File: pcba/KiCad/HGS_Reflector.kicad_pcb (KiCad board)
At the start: 4 copper layers, 100 x 100 mm, 64 parts, among them J1 U.FL, J2 USB_MINI-B_SMT, J3 SM06B-SRSS-TB(LF)(SN), J5 132134-10, J6 132134-10, T1 QWT2.4222, U1 LP2985XX-N, U2 LP2985XX-N, U3 NCS3-272+, U4 QPQ1907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

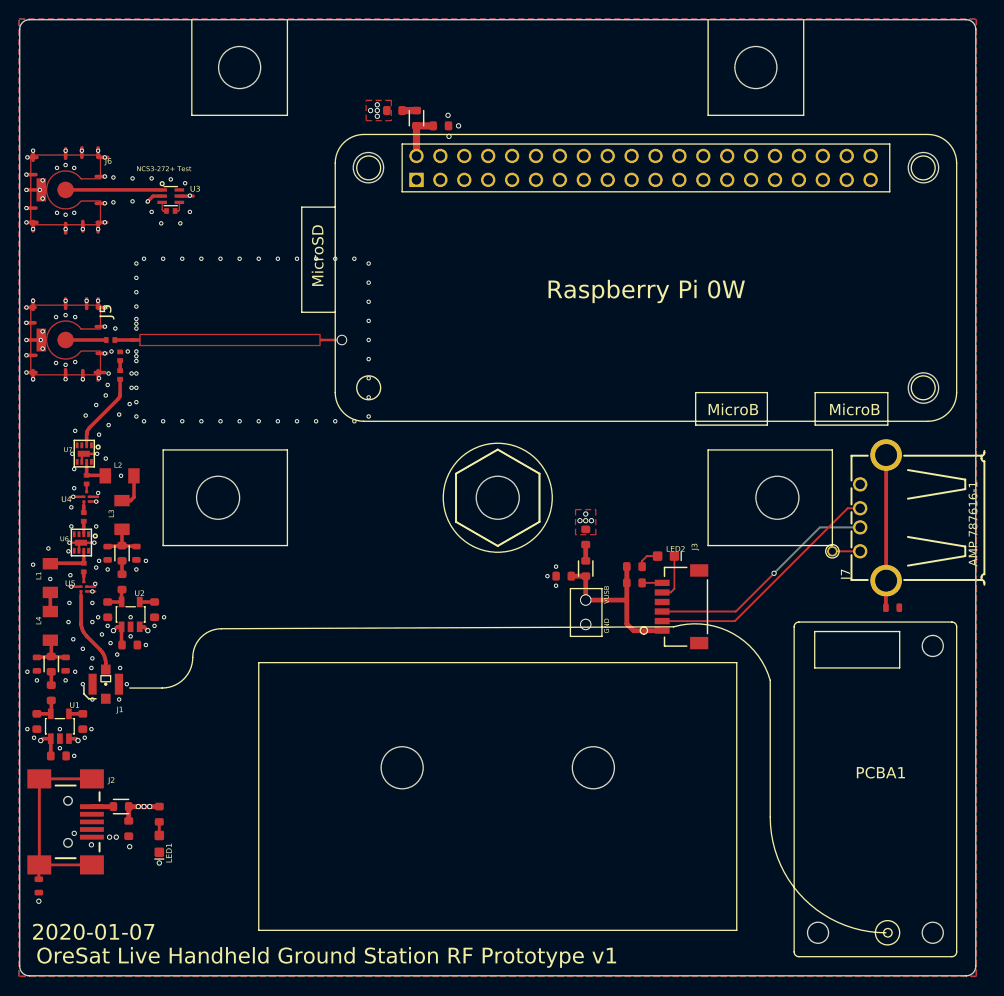
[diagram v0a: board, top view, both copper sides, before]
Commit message: fixed reference designators, fixed symbol/footprint pads and pins, added impedance matching at helical
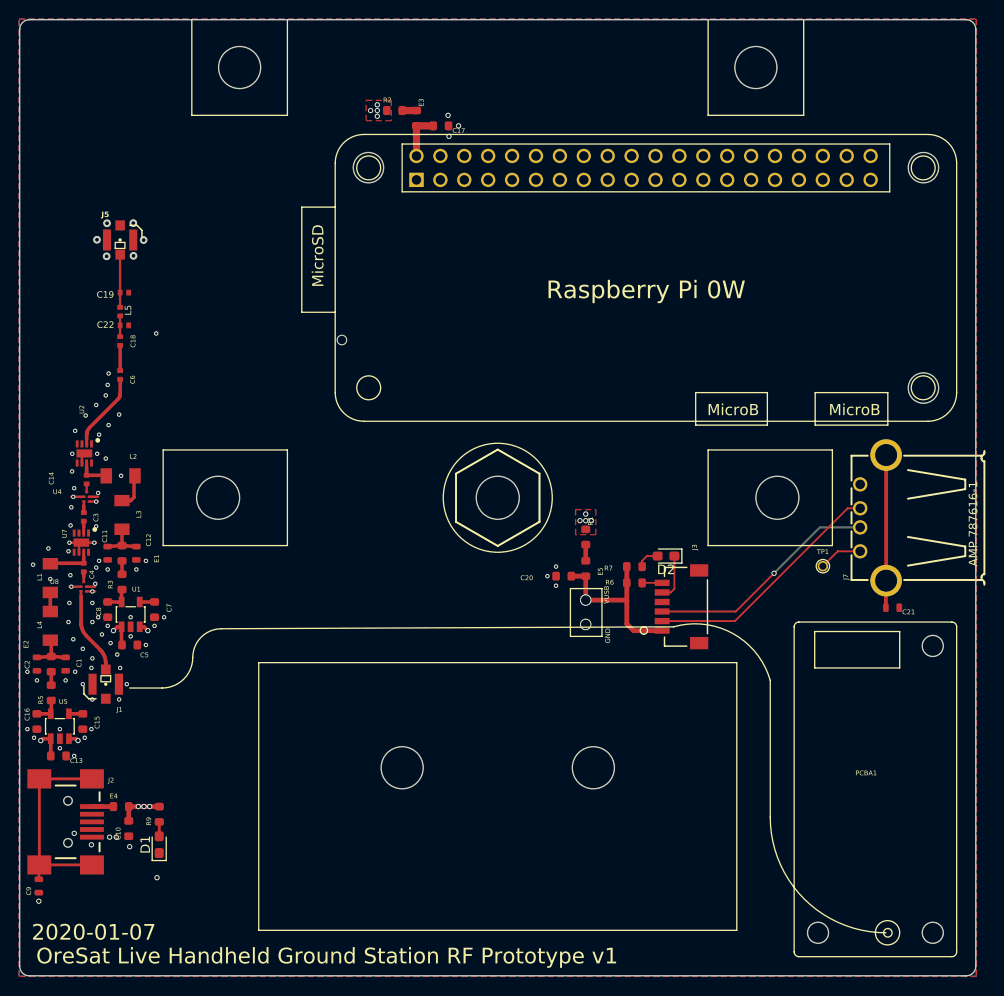
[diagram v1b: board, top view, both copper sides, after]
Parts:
- removed J6: 132134-10, HGS_Reflector:132134-10
- removed LED1, LED2: GREEN, HGS_Reflector:LED-0603
- removed R4: 150, HGS_Reflector:.0402-C-NOSILK
- removed T1: QWT2.4222, HGS_Reflector:QWT_2.422G-V2
- removed TP2: TEST-POINT-LARGE-SQUARE, HGS_Reflector:1X01
- removed U3: NCS3-272+, HGS_Reflector:GE0805C-1
- added C22: 1.0 pF, oresat-passives:0402-C-NOSILK, F.Cu at (109.5, 87.0)
- added D1: Green, LED_SMD:LED_0603_1608Metric_Pad1.05x0.95mm_HandSolder, F.Cu at (113.1, 141.3)
- added D2: Green, LED_SMD:LED_0603_1608Metric_Pad1.05x0.95mm_HandSolder, F.Cu at (166.1, 111.1)
- added L5: 4.3 nH, oresat-passives:0402-C-NOSILK, F.Cu at (109.0, 85.5)
- added TP1: Test-Point, oresat-misc:TestPoint-0.75mm-th, F.Cu at (182.5, 112.2)
- C1, C11, C12, C2, C21, C9: footprint HGS_Reflector:.0603-C-NOSILK -> oresat-passives:0603-C-NOSILK
- C10, C13, C15, C16, C17, C20, C5, C7, C8, R1, R2, R3, R5, R6, R7, R9: footprint HGS_Reflector:.0603-B-NOSILK -> oresat-passives:0603-B-NOSILK
- C14, C18, C3, C4, C6: footprint HGS_Reflector:.0402-C-NOSILK -> oresat-passives:0402-C-NOSILK
- C19: value 100 pF -> 0.9 pF; footprint HGS_Reflector:.0402-C-NOSILK -> oresat-passives:0402-C-NOSILK
- E1, E2, E3, E4, E5: footprint HGS_Reflector:.0603-B -> oresat-passives:0603-B-NOSILK
- J1: footprint HGS_Reflector:U.FL -> oresat-connectors:U.FL
- J2: value USB_MINI-B_SMT -> USB_C_Plug_USB2.0; footprint HGS_Reflector:USB-MINIB -> oresat-connectors:USB-MINIB
- J3: footprint HGS_Reflector:CONN_SM06B-SRSS-TB_JST -> oresat-connectors:CONN_SM06B-SRSS-TB_JST
- J5: footprint HGS_Reflector:132134-10 -> oresat-connectors:U.FL
- J7: value (none) -> USB_HOST_W/CHASSIS_GND; footprint HGS_Reflector:GHI2_USB_HOST_HORIZONTAL_W_CHASSIS_GND -> oresat-misc:GHI2_USB_HOST_HORIZONTAL_W_CHASSIS_GND
- L1, L2, L3, L4: footprint HGS_Reflector:L3216C -> oresat-passives:L3216C
- PCBA2: value (none) -> RASP_PI_0WPI_0W; footprint HGS_Reflector:RASP_PI_0W -> oresat-misc:RASP_PI_0W
- U1: renamed from U2; value LP2985XX-N -> LP2985-N; footprint HGS_Reflector:SOT-23 -> oresat-ics:SOT-23 LP2985
- U2: renamed from U7; value LNA-TP3M9037 -> TQP3M9037; footprint HGS_Reflector:TP3M9037 -> oresat-ics:TQP3M9037
- U4: footprint HGS_Reflector:QPQ1907 -> oresat-ics:QPQ1907
- U5: renamed from U1; value LP2985XX-N -> LP2985-N; footprint HGS_Reflector:SOT-23 -> oresat-ics:SOT-23 LP2985
- U7: renamed from U6; value LNA-TP3M9037 -> TQP3M9037; footprint HGS_Reflector:TP3M9037 -> oresat-ics:TQP3M9037
- U8: renamed from U5; value QPQ1907 -> B39162B9417K610; footprint HGS_Reflector:QPQ1907 -> oresat-ics:QPQ1907
- moved J5 11.9 mm to (109.0, 78.0)
- moved C19 6.68 mm to (109.5, 83.5), turned to 180 degrees
- moved C18 1.00 mm to (109.0, 88.6), turned to 90 degrees
- moved L2 0.11 mm to (109.1, 102.7)
- moved U2 0.07 mm to (105.3, 100.4), turned to -90 degrees
- turned U7 to -90 degrees
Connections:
- net N$12 renamed VBUS
- C14 pad 1: N$16 -> Net-(U2-RF_OUT)
- C14 pad 2: N$26 -> Net-(U4-IN)
- C18 pad 1: HELICAL -> Net-(C18-Pad1)
- C18 pad 2: T1-50 -> Net-(C18-Pad2)
- C19 pad 2: N$9 -> Net-(J5-SIGNAL)
- C3 pad 1: N$4 -> Net-(U4-OUT)
- C3 pad 2: N$8 -> Net-(U7-RF_IN)
- C4 pad 1: N$13 -> Net-(U7-RF_OUT)
- C4 pad 2: N$3 -> Net-(U8-IN)
- C6 pad 1: N$9 -> Net-(C18-Pad1)
- C6 pad 2: N$11 -> Net-(U2-RF_IN)
- C9 pad 2: KEEPOUT -> Net-(J2-SHIELD)
- E4 pad 1: VUSB -> Net-(E4-Pad1)
- J1 pad FEED: N$5 -> Net-(J1-SIGNAL)
- J2 pad S1: KEEPOUT -> Net-(J2-SHIELD)
- L1 pad 1: N$13 -> Net-(U7-RF_OUT)
- L2 pad 1: N$16 -> Net-(U2-RF_OUT)
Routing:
- net GND: track 49.6 -> 10.9 mm, vias 201 -> 91
- net Net-(J2-SHIELD): track 0.00 -> 24.0 mm
- net KEEPOUT: track 24.0 -> 0.00 mm
- net N$23: track 10.1 -> 0.00 mm
- net Net-(J1-SIGNAL): track 0.00 -> 9.10 mm
- net N$5: track 9.10 -> 0.00 mm
- net Net-(U2-RF_IN): track 0.00 -> 8.29 mm
- net N$11: track 8.29 -> 0.00 mm
- net Net-(J5-SIGNAL): track 0.00 -> 5.52 mm
- net Net-(U7-RF_OUT): track 0.00 -> 4.82 mm
- net N$13: track 4.82 -> 0.00 mm
- net T1-50: track 4.25 -> 0.00 mm
- net Net-(U2-RF_OUT): track 0.00 -> 3.37 mm
- net N$16: track 3.37 -> 0.00 mm
- net Net-(C18-Pad1): track 0.00 -> 2.65 mm
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- removed copper zone on In2.Cu, net GND
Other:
- board text removed: "NCS3-272+ Test"

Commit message: organized schematic
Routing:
- net GND: vias 91 -> 107
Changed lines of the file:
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@@
 		(descr "<b>0402 (metric 1005) tight 'IPC-C' without silkscreen</b>\n<br>In house package for minimum spacing based on IPC-7351B.\nThis package is identical to 0402-C, but has its tPlace silkscreen layer removed.")
 		(property "Reference" "C19"
-			(at 1.07 0.17 360)
+			(at 1.07 0.17 0)
 			(layer "F.SilkS")
 			(effects
@@
 		)
 		(property "Value" "0.9 pF"
-			(at -0.7 1.25 360)
+			(at -0.7 1.25 0)
 			(layer "F.Fab")
 			(effects
@@
 		)
 		(property "Footprint" "oresat-passives:0402-C-NOSILK"
-			(at 0 0 360)
+			(at 0 0 0)
 			(layer "F.Fab")
 			(hide yes)
@@
 		)
 		(property "Datasheet" ""
-			(at 0 0 360)
+			(at 0 0 0)
 			(layer "F.Fab")
 			(hide yes)
@@
 		)
 		(property "Description" ""
-			(at 0 0 360)
+			(at 0 0 0)
 			(layer "F.Fab")
 			(hide yes)
@@
 		(descr "<b>0402 (metric 1005) tight 'IPC-C' without silkscreen</b>\n<br>In house package for minimum spacing based on IPC-7351B.\nThis package is identical to 0402-C, but has its tPlace silkscreen layer removed.")
 		(property "Reference" "C18"
-			(at -0.7 1.66 90)
+			(at -0.65 2.45 90)
 			(layer "F.SilkS")
 			(effects
@@
 		(tags "LED handsolder")
 		(property "Reference" "D2"
-			(at 0 -1.43 360)
+			(at 0 -1.43 0)
 			(layer "F.SilkS")
 			(effects
@@
 		)
 		(property "Value" "Green"
-			(at 0 1.43 360)
+			(at 0 1.43 0)
 			(layer "F.Fab")
 			(effects
@@
 		)
 		(fp_text user "${REFERENCE}"
-			(at 0 0 360)
+			(at 0 0 0)
 			(layer "F.Fab")
 			(effects
@@
 		(at 108.9989 78.04 -90)
 		(property "Reference" "J5"
-			(at -2.66 1.13 360)
+			(at -2.66 1.13 0)
 			(layer "F.SilkS")
 			(effects
@@
 	)
 	(via
+		(at 109.9 87.72)
+		(size 0.4572)
+		(drill 0.254)
+		(layers "F.Cu" "B.Cu")
+		(net 1)
+	)
+	(via
 		(at 106.5011 95.3036)
 		(size 0.4572)
@@
 	)
 	(via
+		(at 108.41 81.01)
+		(size 0.4572)
+		(drill 0.254)
+		(layers "F.Cu" "B.Cu")
+		(net 1)
+	)
+	(via
 		(at 106.1011 114.8036)
 		(size 0.4572)
@@
 	)
 	(via
+		(at 109.64 81.01)
+		(size 0.4572)
+		(drill 0.254)
+		(layers "F.Cu" "B.Cu")
+		(net 1)
+	)
+	(via
 		(at 102.7011 131.2036)
 		(size 0.4572)
@@
 	)
 	(via
+		(at 109.61 81.95)
+		(size 0.4572)
+		(drill 0.254)
+		(layers "F.Cu" "B.Cu")
+		(net 1)
+	)
+	(via
 		(at 112.78 87.82)
 		(size 0.4572)
@@
 	)
 	(via
+		(at 109.91 84.28)
+		(size 0.4572)
+		(drill 0.254)
+		(layers "F.Cu" "B.Cu")
+		(net 1)
+	)
+	(via
 		(at 103.6011 118.0036)
 		(size 0.4572)
@@
 	)
 	(via
+		(at 108.41 81.95)
+		(size 0.4572)
+		(drill 0.254)
+		(layers "F.Cu" "B.Cu")
+		(net 1)
+	)
+	(via
 		(at 106.5825 78.0189)
 		(size 0.8)
@@
 	)
 	(via
+		(at 109.85 89.87)
+		(size 0.4572)
+		(drill 0.254)
+		(layers "F.Cu" "B.Cu")
+		(net 1)
+	)
+	(via
 		(at 106.5011 112.3036)
 		(size 0.4572)
@@
 	)
 	(via
+		(at 109.76 93.63)
+		(size 0.4572)
+		(drill 0.254)
+		(layers "F.Cu" "B.Cu")
+		(net 1)
+	)
+	(via
 		(at 112.86 144.74)
 		(size 0.5532)
@@
 	)
 	(via
+		(at 109.68 94.83)
+		(size 0.4572)
+		(drill 0.254)
+		(layers "F.Cu" "B.Cu")
+		(net 1)
+	)
+	(via
 		(at 106.5011 108.0036)
 		(size 0.4572)
@@
 	)
 	(via
+		(at 110.61 86.98)
+		(size 0.4572)
+		(drill 0.254)
+		(layers "F.Cu" "B.Cu")
+		(net 1)
+	)
+	(via
 		(at 108.7011 121.4036)
 		(size 0.4572)
@@
 	)
 	(via
+		(at 109.93 86.23)
+		(size 0.4572)
+		(drill 0.254)
+		(layers "F.Cu" "B.Cu")
+		(net 1)
+	)
+	(via
 		(at 106.0011 141.3036)
 		(size 0.5532)
@@
 	)
 	(via
+		(at 110.62 83.56)
+		(size 0.4572)
+		(drill 0.254)
+		(layers "F.Cu" "B.Cu")
+		(net 1)
+	)
+	(via
 		(at 110.0011 141.5036)
 		(size 0.5532)
@@
 	)
 	(via
+		(at 108.12 90.79)
+		(size 0.4572)
+		(drill 0.254)
+		(layers "F.Cu" "B.Cu")
+		(net 1)
+	)
+	(via
 		(at 101.7011 113.5036)
 		(size 0.4572)
@@
 	)
 	(via
+		(at 109.86 90.79)
+		(size 0.4572)
+		(drill 0.254)
+		(layers "F.Cu" "B.Cu")
+		(net 1)
+	)
+	(via
 		(at 103.9011 106.0036)
 		(size 0.4572)
@@
 	)
 	(via
+		(at 109.92 82.81)
+		(size 0.4572)
+		(drill 0.254)
+		(layers "F.Cu" "B.Cu")
+		(net 1)
+	)
+	(via
 		(at 103.7011 109.7036)
 		(size 0.4572)
 		(drill 0.254)
+		(layers "F.Cu" "B.Cu")
+		(net 1)
+	)
+	(via
+		(at 108.15 89.87)
+		(size 0.4572)
+		(drill 0.254)

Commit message: minor layout changes
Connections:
- net Net-(C18-Pad2) renamed /RF2
- net Net-(J5-SIGNAL) renamed /RF1
- net Net-(U2-RF_IN) renamed /RF3
- net Net-(U2-RF_OUT) renamed /RF4
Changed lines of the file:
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@@
 	(net 7 "VBUS")
 	(net 8 "Net-(C18-Pad1)")
-	(net 9 "Net-(U2-RF_IN)")
+	(net 9 "/RF3")
 	(net 10 "Net-(U1-BYPASS)")
 	(net 11 "Net-(U1-VOUT)")
@@
 	(net 13 "Net-(C11-Pad1)")
 	(net 14 "Net-(U4-IN)")
-	(net 15 "Net-(U2-RF_OUT)")
+	(net 15 "/RF4")
 	(net 16 "Net-(U5-BYPASS)")
 	(net 17 "Net-(U5-VOUT)")
@@
 	(net 25 "Net-(E5-Pad1)")
 	(net 26 "Net-(J1-SIGNAL)")
-	(net 27 "Net-(C18-Pad2)")
+	(net 27 "/RF2")
 	(net 28 "Net-(J7-D-)")
 	(net 29 "Net-(J3-Pad6)")
@@
 	(net 44 "unconnected-(J2-D+-PadA6)")
 	(net 45 "unconnected-(J2-D--PadA7)")
-	(net 46 "Net-(J5-SIGNAL)")
+	(net 46 "/RF1")
 	(net 47 "Net-(D1-A)")
 	(net 48 "Net-(D2-A)")
@@
 			(layers "F.Cu" "F.Paste")
 			(roundrect_rratio 0.1)
-			(net 15 "Net-(U2-RF_OUT)")
+			(net 15 "/RF4")
 			(pintype "passive")
 			(solder_mask_margin 0.1016)
@@
 			(layers "F.Cu" "F.Paste")
 			(roundrect_rratio 0.1)
-			(net 46 "Net-(J5-SIGNAL)")
+			(net 46 "/RF1")
 			(pintype "passive")
 			(solder_mask_margin 0.1016)
@@
 			(layers "F.Cu" "F.Paste")
 			(roundrect_rratio 0.1)
-			(net 27 "Net-(C18-Pad2)")
+			(net 27 "/RF2")
 			(pintype "passive")
 			(solder_mask_margin 0.1016)
@@
 			(layers "F.Cu" "F.Paste")
 			(roundrect_rratio 0.1)
-			(net 46 "Net-(J5-SIGNAL)")
+			(net 46 "/RF1")
 			(pinfunction "1")
 			(pintype "passive")
@@
 			(layers "F.Cu" "F.Paste")
 			(roundrect_rratio 0.1)
-			(net 27 "Net-(C18-Pad2)")
+			(net 27 "/RF2")
 			(pinfunction "2")
 			(pintype "passive")
@@
 			(layers "F.Cu" "F.Paste")
 			(roundrect_rratio 0.1)
-			(net 27 "Net-(C18-Pad2)")
+			(net 27 "/RF2")
 			(pintype "passive")
 			(solder_mask_margin 0.1016)
@@
 			(size 1.05 1)
 			(layers "F.Cu" "F.Paste" "F.Mask")
-			(net 46 "Net-(J5-SIGNAL)")
+			(net 46 "/RF1")
 			(pinfunction "SIGNAL")
 			(pintype "bidirectional")
@@
 			(size 1.2 1.6)
 			(layers "F.Cu" "F.Paste" "F.Mask")
-			(net 15 "Net-(U2-RF_OUT)")
+			(net 15 "/RF4")
 			(pintype "passive")
 			(solder_mask_margin 0.0635)
@@
 			(size 0.3 0.75)
 			(layers "F.Cu" "F.Paste" "F.Mask")
-			(net 9 "Net-(U2-RF_IN)")
+			(net 9 "/RF3")
 			(pinfunction "RF_IN")
 			(pintype "passive")
@@
 			(size 0.3 0.75)
 			(layers "F.Cu" "F.Paste" "F.Mask")
-			(net 15 "Net-(U2-RF_OUT)")
+			(net 15 "/RF4")
 			(pinfunction "RF_OUT")
 			(pintype "passive")
@@
 			(layers "F.Cu" "F.Paste")
 			(roundrect_rratio 0.1)
-			(net 9 "Net-(U2-RF_IN)")
+			(net 9 "/RF3")
 			(pintype "passive")
 			(solder_mask_margin 0.1016)
@@
 		(start 108.9989 83.5389)
 		(end 109 83.54)
-		(width 0.25)
+		(width 0.127)
 		(layer "F.Cu")
 		(net 46)
@@
 		(start 108.9989 79.565)
 		(end 108.9989 83.5389)
-		(width 0.25)
+		(width 0.127)
 		(layer "F.Cu")
 		(net 46)

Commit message: added connection from rf track to helical at entry point
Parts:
- added J4: Conn_01x01_Pin, TestPoint:TestPoint_THTPad_D1.5mm_Drill0.7mm, F.Cu at (132.2, 88.5)
- added R4: R_Small_US, oresat-passives:0402-C-NOSILK, F.Cu at (106.3, 88.2)
- moved C19 7.73 mm to (105.9, 90.4)
- moved C18 7.26 mm to (105.5, 95.0)
- moved C22 7.26 mm to (105.9, 93.3)
- moved L5 7.26 mm to (105.5, 91.9)
- moved C6 5.95 mm to (105.5, 96.9)
- moved J5 5.93 mm to (106.3, 83.3)
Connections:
- J5 pad FEED: /RF1 -> Net-(J5-SIGNAL)
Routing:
- net /RF1: track 5.52 -> 29.3 mm
- net /RF3: track 8.29 -> 1.99 mm
- net Net-(J5-SIGNAL): track 0.00 -> 2.84 mm
- net Net-(C18-Pad1): track 2.65 -> 1.09 mm
- net GND: vias 107 -> 117
- net (no net): vias 1 -> 0
